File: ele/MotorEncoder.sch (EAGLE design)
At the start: 18 parts, among them X1 PHB_1MM27_2X03_SNT_S, X2 PHB_1MM27_2X03_SNT_S

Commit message: ele: MotorEncoder - finish layout of PCB
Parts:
- removed C3: 100n/6,3V,, rcl:C-EUC0603
- removed JP1: HAL_TOP, pinhead:PINHD-1X3/90
- removed JP2: HAL_SIDE_R, pinhead:PINHD-1X3/90
- removed JP4, JP5: HAL_SIDE_L, pinhead:PINHD-1X3/90
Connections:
- removed net HAL_SIDE: JP2.3, JP3.1, JP4.3, R3.1, R5.1, X2-5.S, X2-6.S
- removed net HAL_TOP: JP1.3, JP3.2, R2.1, R4.1, X1-5.S, X1-6.S
- new net HAL_LEFT: JP3.2, R2.1, R4.1, X1-2.S, X1-5.S
- new net HAL_RIGHT: JP3.1, R3.1, R5.1, X2-2.S, X2-5.S
- net +5V: now also X1-6.S, X2-6.S; no longer C3.1, JP1.1, JP2.1, JP4.1, X1-2.S, X2-2.S
- net GND: no longer C3.2, JP1.2, JP2.2, JP4.2
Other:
- moved on the sheet: X1-2, X1-6, X2-2, X2-6

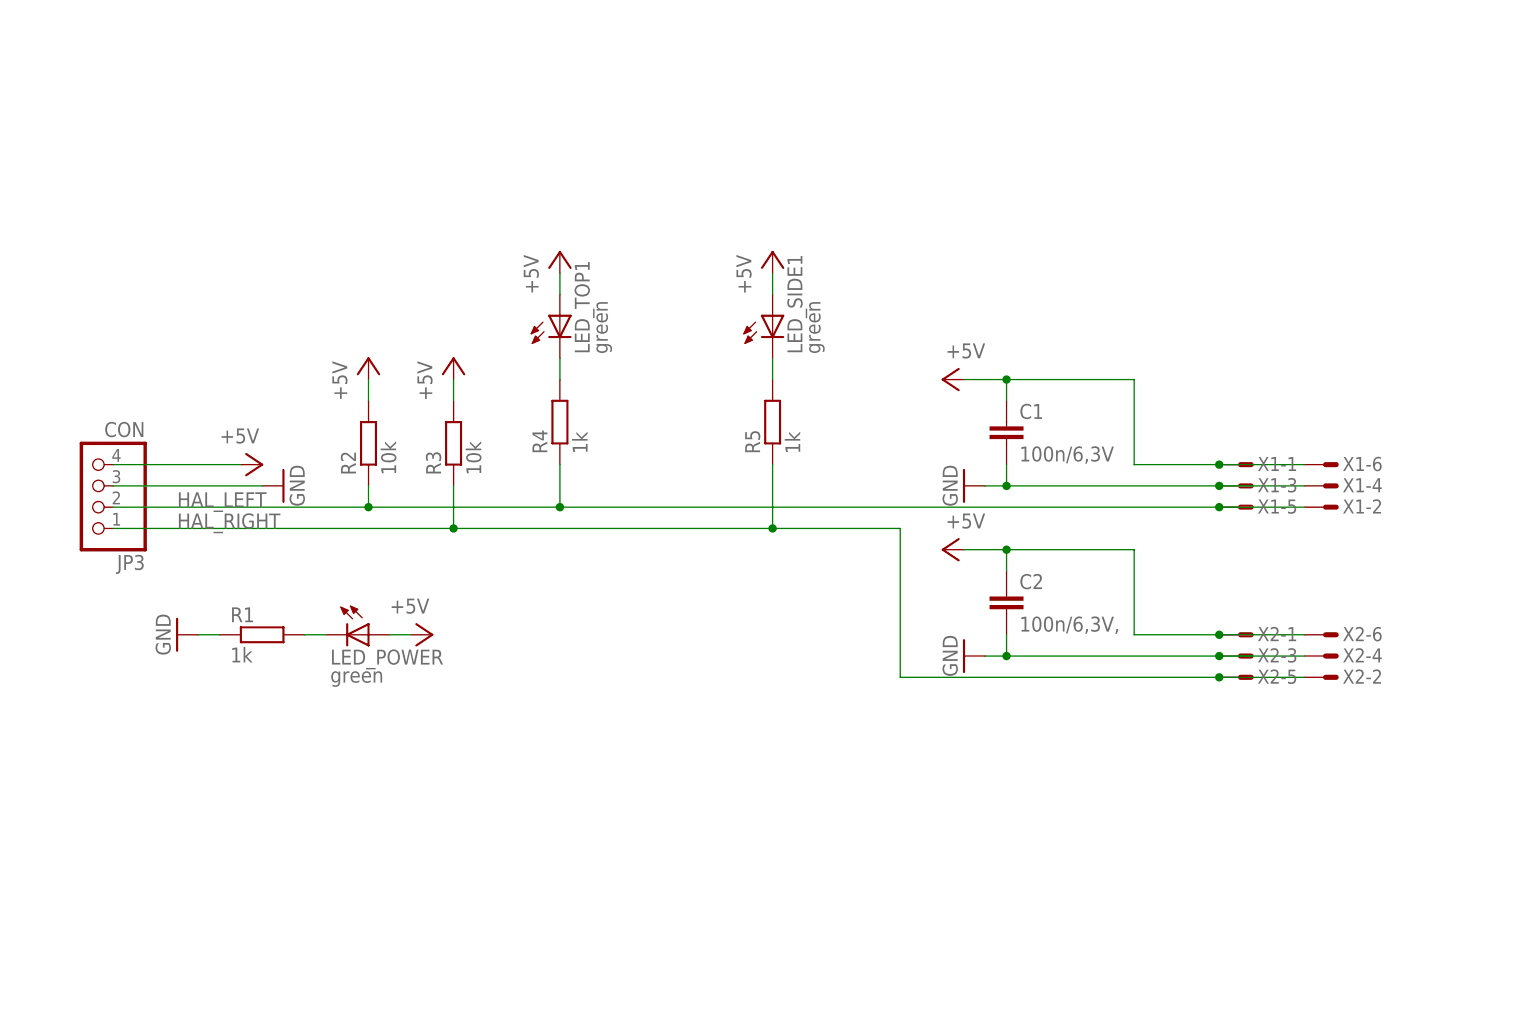
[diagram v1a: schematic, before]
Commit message: Add licenses to Eagle files
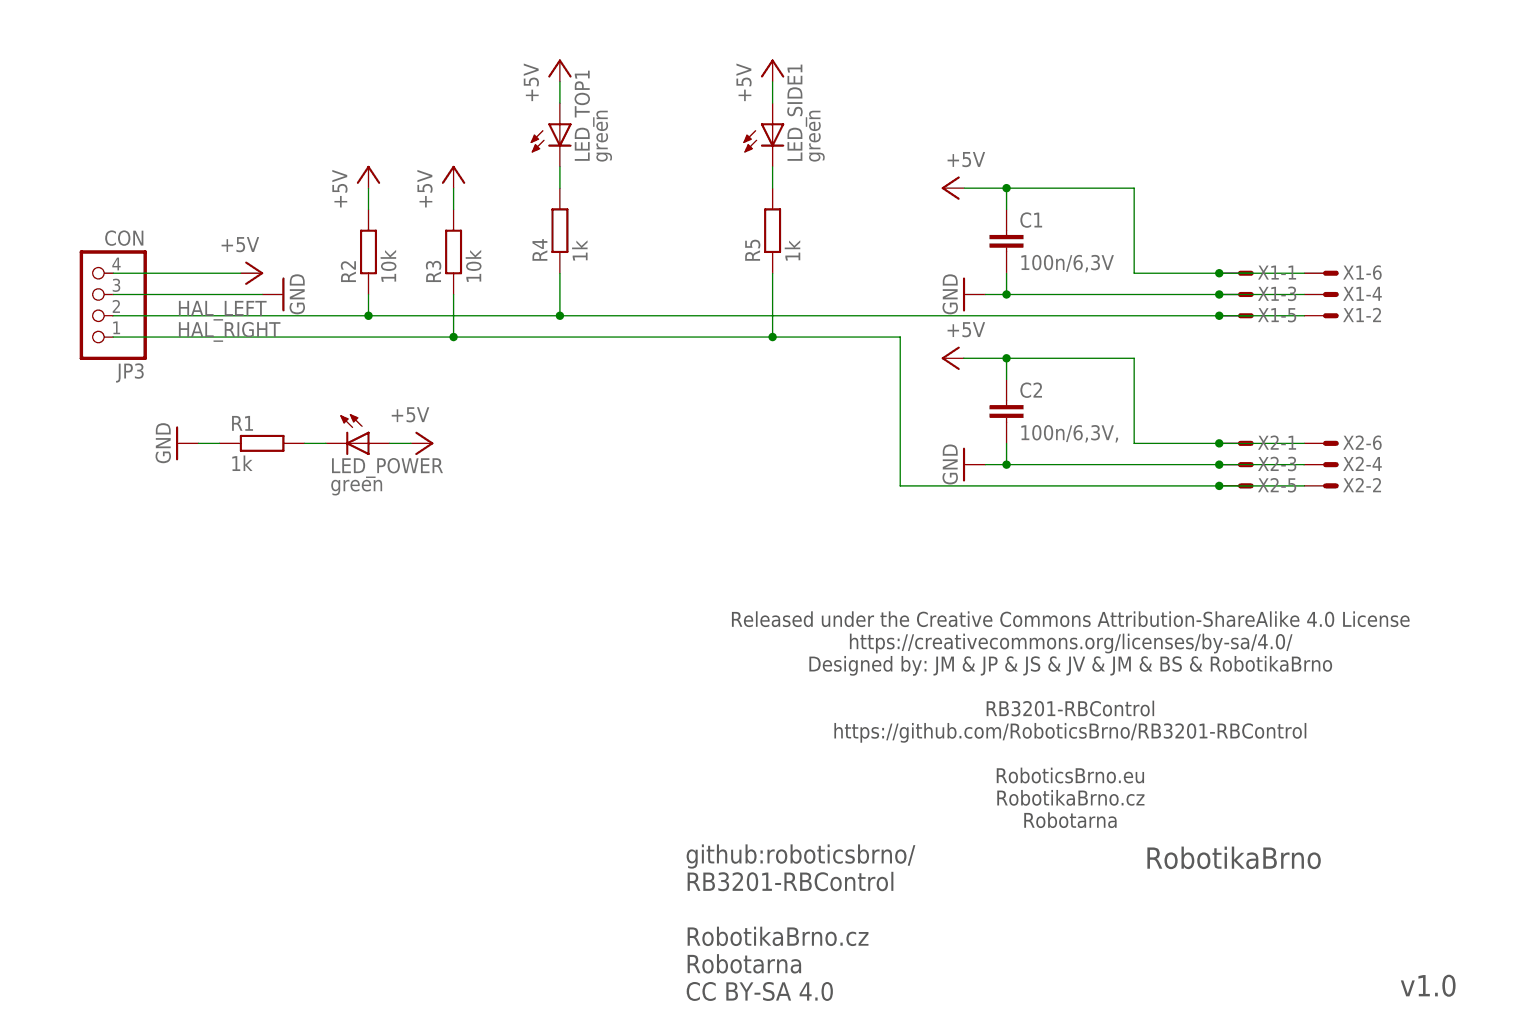
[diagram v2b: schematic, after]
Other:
- note added: "Released under the Creative Commons Attribution-ShareAlike 4.0 License https://creativecommons.org/licenses/by-sa/4.0/ Designed by: JM & JP & JS & JV & JM & BS & RobotikaBrno RB3201-RBControl https://github.com/RoboticsBrno/RB3201-RBControl RoboticsBrno.eu RobotikaBrno.cz Robotarna"
- note added: "RobotikaBrno"
- note added: "github:roboticsbrno/ RB3201-RBControl RobotikaBrno.cz Robotarna CC BY-SA 4.0"
- note added: "v1.0"
- moved on the sheet: C1, C2, JP3, LED_POWER, LED_SIDE1, LED_TOP1, R1, R2, R3, R4, R5, X1-1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

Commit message: ele: Reroute MotorEncoder
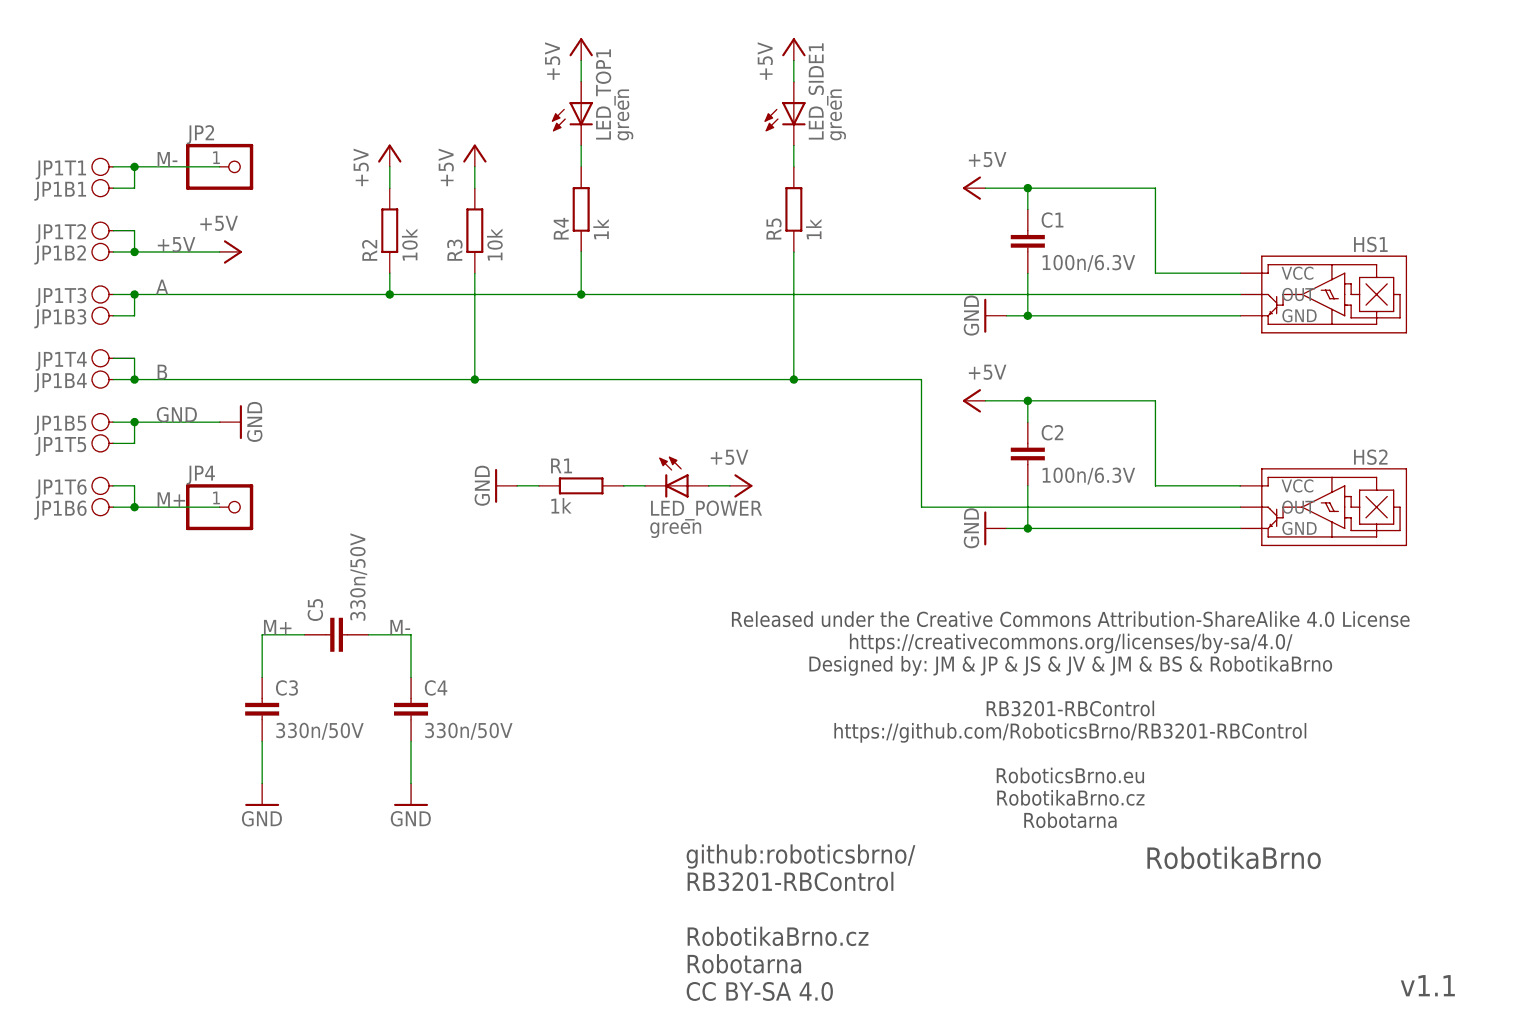
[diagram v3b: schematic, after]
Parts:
- removed JP3: CON, pinhead:PINHD-1X4/90
- removed X1, X2: PHB_1MM27_2X03_SNT_S, _hhn_con_pinhead_box_1mm27:PHB_1MM27_2X03_SNT_S
- added C3, C4, C5: 330n/50V, rcl:C-EUC0805
- added HS1, HS2: (no value), HallSensor:HALL
- added JP1: PINH2X06, pinhead_smd:PINH2X06
- added JP2, JP4: (no value), pinhead:PINHD-1X1
- C1: value 100n/6,3V -> 100n/6.3V; device rcl:C-EUC0603 -> rcl:C-EUC0402
- C2: value 100n/6,3V, -> 100n/6.3V; device rcl:C-EUC0603 -> rcl:C-EUC0402
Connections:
- removed net HAL_LEFT: JP3.2, R2.1, R4.1, X1-2.S, X1-5.S
- removed net HAL_RIGHT: JP3.1, R3.1, R5.1, X2-2.S, X2-5.S
- new net A: HS1.OUT, JP1B3.1, JP1T3.1, R2.1, R4.1
- new net B: HS2.OUT, JP1B4.1, JP1T4.1, R3.1, R5.1
- new net M+: C3.1, C5.1, JP1B6.1, JP1T6.1, JP4.1
- new net M-: C4.1, C5.2, JP1B1.1, JP1T1.1, JP2.1
- net +5V: now also HS1.VCC, HS2.VCC, JP1B2.1, JP1T2.1; no longer JP3.4, X1-1.S, X1-6.S, X2-1.S, X2-6.S
- net GND: now also C3.2, C4.2, HS1.GND, HS2.GND, JP1B5.1, JP1T5.1; no longer JP3.3, X1-3.S, X1-4.S, X2-3.S, X2-4.S
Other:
- note added: "v1.1"
- note removed: "v1.0"
- moved on the sheet: C1, C2, LED_POWER, LED_SIDE1, LED_TOP1, R1, R2, R3, R4, R5
